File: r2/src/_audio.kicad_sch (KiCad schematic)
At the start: 27 parts, among them J1 532610271, J5 PJ-320D, U4 PCM5100APW, U5 PAM8908

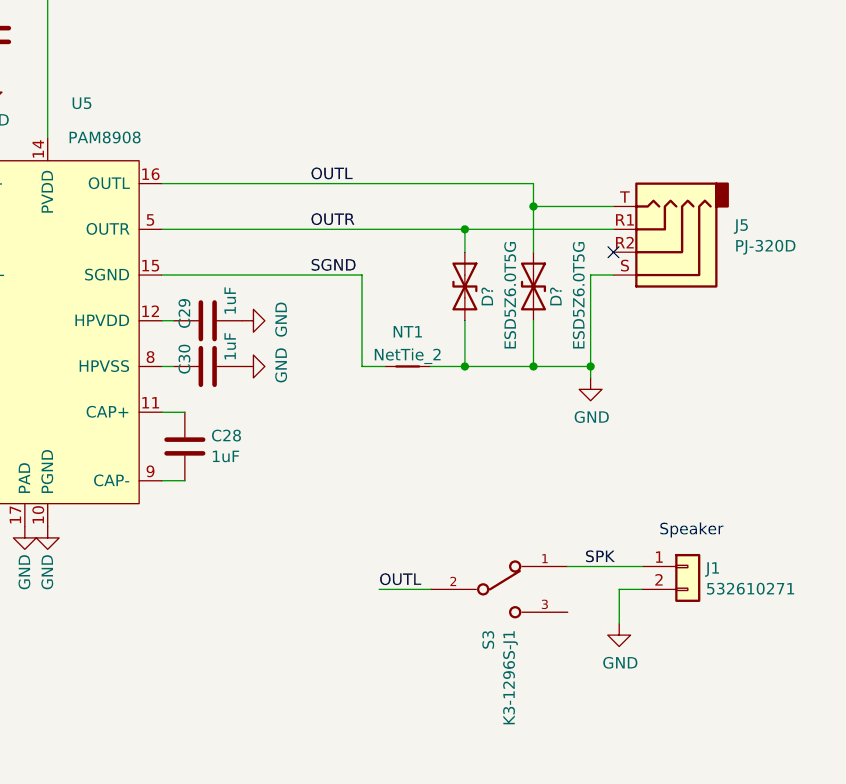
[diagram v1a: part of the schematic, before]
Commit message: Correct switch symbol so default switch behaviour from factory is correctly shown.
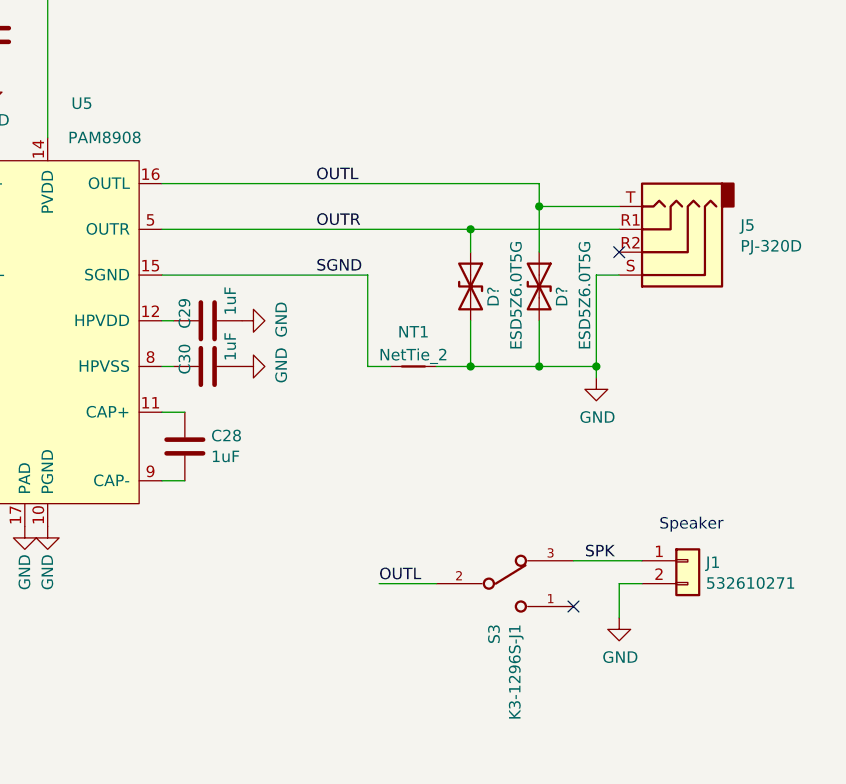
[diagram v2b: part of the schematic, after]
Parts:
- S3: symbol j_Switch:JS102011SAQN -> j_Switch:K3-1296S; MPN K3-1296S-J1 -> K3-1296S
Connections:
- net SPK: now also S3.3; no longer S3.1
- no-connect marks 1 -> 2
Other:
- moved on the sheet: D?, J1, J5, NT1, S3

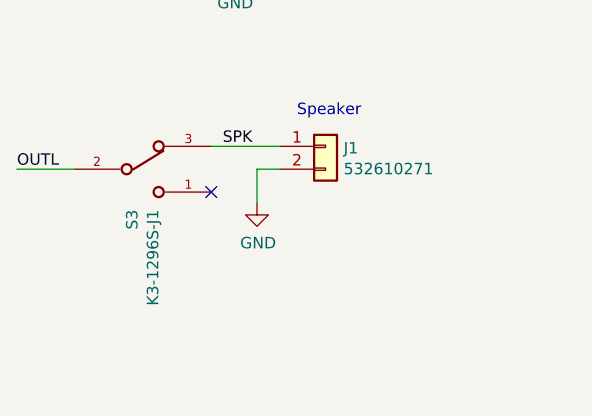
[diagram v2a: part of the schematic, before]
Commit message: Change speaker connector symbol to include mounting pads. Add speaker symbol and footprint
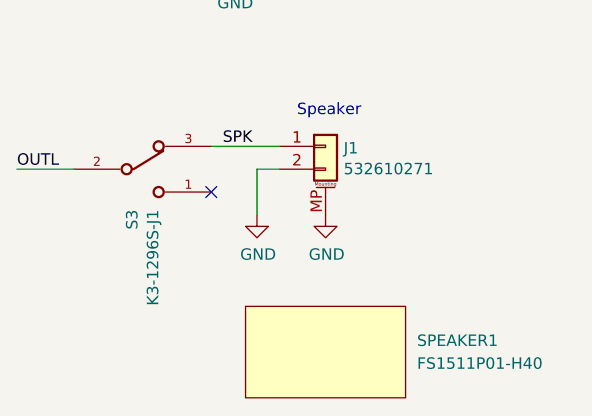
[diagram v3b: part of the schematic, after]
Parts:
- added SPEAKER1: FS1511P01-H40, jeffmakes-footprints:FS1511P01-Hx-Lx, symbol j_Display:Display_dummy
- J1: symbol Connector_Generic:Conn_01x02 -> Connector_Generic_MountingPin:Conn_01x02_MountingPin
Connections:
- net GND: now also J1.MP (MountPin)
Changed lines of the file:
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@@
     (stroke (width 0) (type default))
   )
-  (wire (pts (xy 243.84 127) (xy 243.84 130.81))
+  (wire (pts (xy 243.84 127) (xy 243.84 132.08))
     (stroke (width 0) (type default))
   )
@@
     )
   )
-  (symbol (lib_id "power:GND") (at 243.84 130.81 0) (unit 1)
-    (in_bom yes) (on_board yes) (dnp no)
-    (property "Reference" "#PWR0154" (at 243.84 137.16 0)
-      (effects (font (size 1.27 1.27)) hide)
-    )
-    (property "Value" "GND" (at 243.967 135.2042 0)
-      (effects (font (size 1.27 1.27)))
-    )
-    (property "Footprint" "" (at 243.84 130.81 0)
-      (effects (font (size 1.27 1.27)) hide)
-    )
-    (property "Datasheet" "" (at 243.84 130.81 0)
+  (symbol (lib_id "power:GND") (at 251.46 132.08 0) (unit 1)
+    (in_bom yes) (on_board yes) (dnp no)
+    (property "Reference" "#PWR0155" (at 251.46 138.43 0)
+      (effects (font (size 1.27 1.27)) hide)
+    )
+    (property "Value" "GND" (at 251.587 136.4742 0)
+      (effects (font (size 1.27 1.27)))
+    )
+    (property "Footprint" "" (at 251.46 132.08 0)
+      (effects (font (size 1.27 1.27)) hide)
+    )
+    (property "Datasheet" "" (at 251.46 132.08 0)
+      (effects (font (size 1.27 1.27)) hide)
+    )
+    (pin "1")
+    (instances
+      (project "tr23-badge-r2"
+        (path "/ab725fe7-4504-40ef-b6af-82d065d00fb6/00000000-0000-0000-0000-00005dd6a7f2"
+          (reference "#PWR0155") (unit 1)
+        )
+      )
+    )
+  )
+  (symbol (lib_id "power:GND") (at 243.84 132.08 0) (unit 1)
+    (in_bom yes) (on_board yes) (dnp no)
+    (property "Reference" "#PWR0154" (at 243.84 138.43 0)
+      (effects (font (size 1.27 1.27)) hide)
+    )
+    (property "Value" "GND" (at 243.967 136.4742 0)
+      (effects (font (size 1.27 1.27)))
+    )
+    (property "Footprint" "" (at 243.84 132.08 0)
+      (effects (font (size 1.27 1.27)) hide)
+    )
+    (property "Datasheet" "" (at 243.84 132.08 0)
       (effects (font (size 1.27 1.27)) hide)
     )
@@
     )
   )
-  (symbol (lib_id "Connector_Generic:Conn_01x02") (at 251.46 124.46 0) (unit 1)
+  (symbol (lib_id "j_Display:Display_dummy") (at 251.46 147.32 0) (unit 1)
+    (in_bom yes) (on_board yes) (dnp no) (fields_autoplaced)
+    (property "Reference" "SPEAKER1" (at 261.62 146.05 0)
+      (effects (font (size 1.27 1.27)) (justify left))
+    )
+    (property "Value" "FS1511P01-H40" (at 261.62 148.59 0)
+      (effects (font (size 1.27 1.27)) (justify left))
+    )
+    (property "Footprint" "jeffmakes-footprints:FS1511P01-Hx-Lx" (at 251.46 147.32 0)
+      (effects (font (size 1.27 1.27)) hide)
+    )
+    (property "Datasheet" "" (at 251.46 147.32 0)
+      (effects (font (size 1.27 1.27)) hide)
+    )
+    (instances
+      (project "tr23-badge-r2"
+        (path "/ab725fe7-4504-40ef-b6af-82d065d00fb6/00000000-0000-0000-0000-00005dd6a7f2"
+          (reference "SPEAKER1") (unit 1)
+        )
+      )
+    )
+  )
+  (symbol (lib_id "Connector_Generic_MountingPin:Conn_01x02_MountingPin") (at 251.46 124.46 0) (unit 1)
     (in_bom yes) (on_board yes) (dnp no)
     (property "Reference" "J1" (at 253.4666 124.6632 0)
@@
     (pin "1")
     (pin "2")
-    (instances
-      (project "tr23-badge-r2"
+    (pin "MP")
+    (instances
+      (project "tr23-badge-r2"

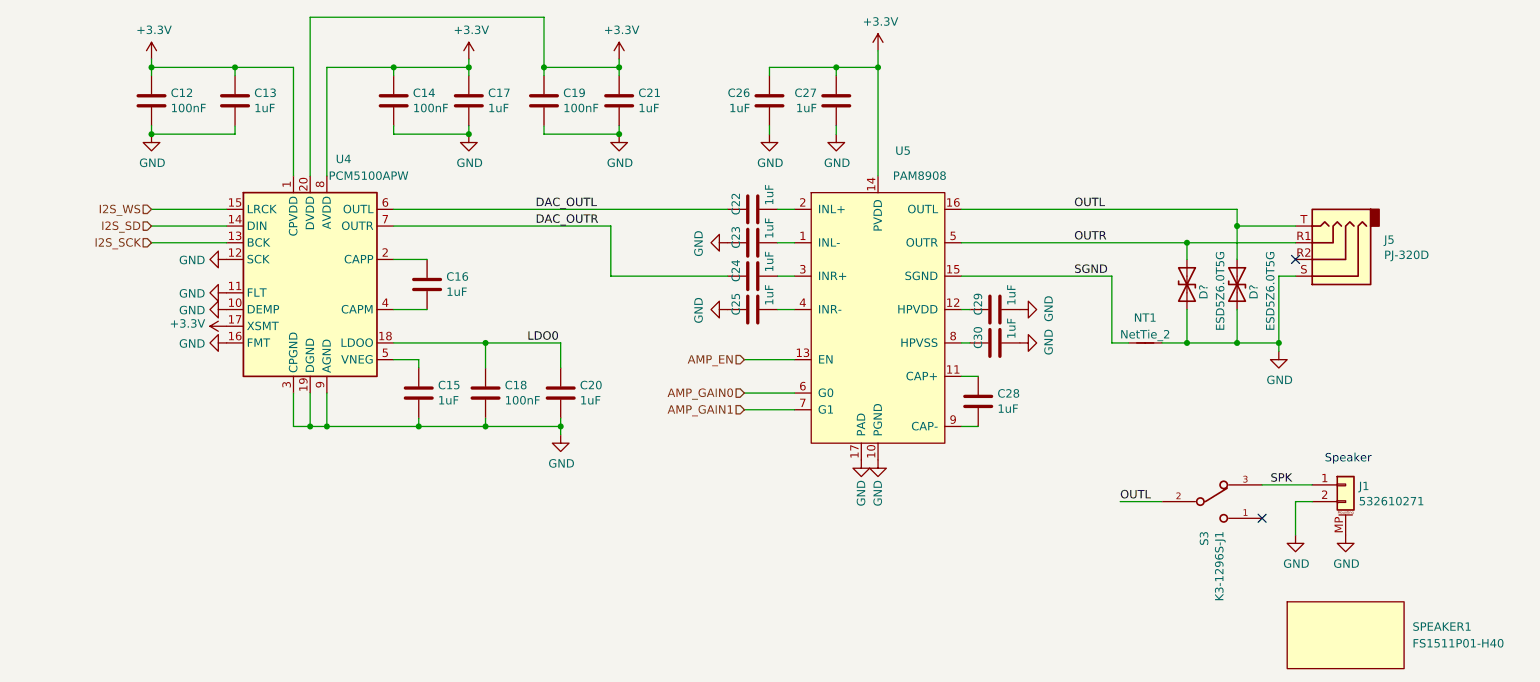
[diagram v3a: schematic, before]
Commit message: Add pull-downs to amplifier enable/gain control lines
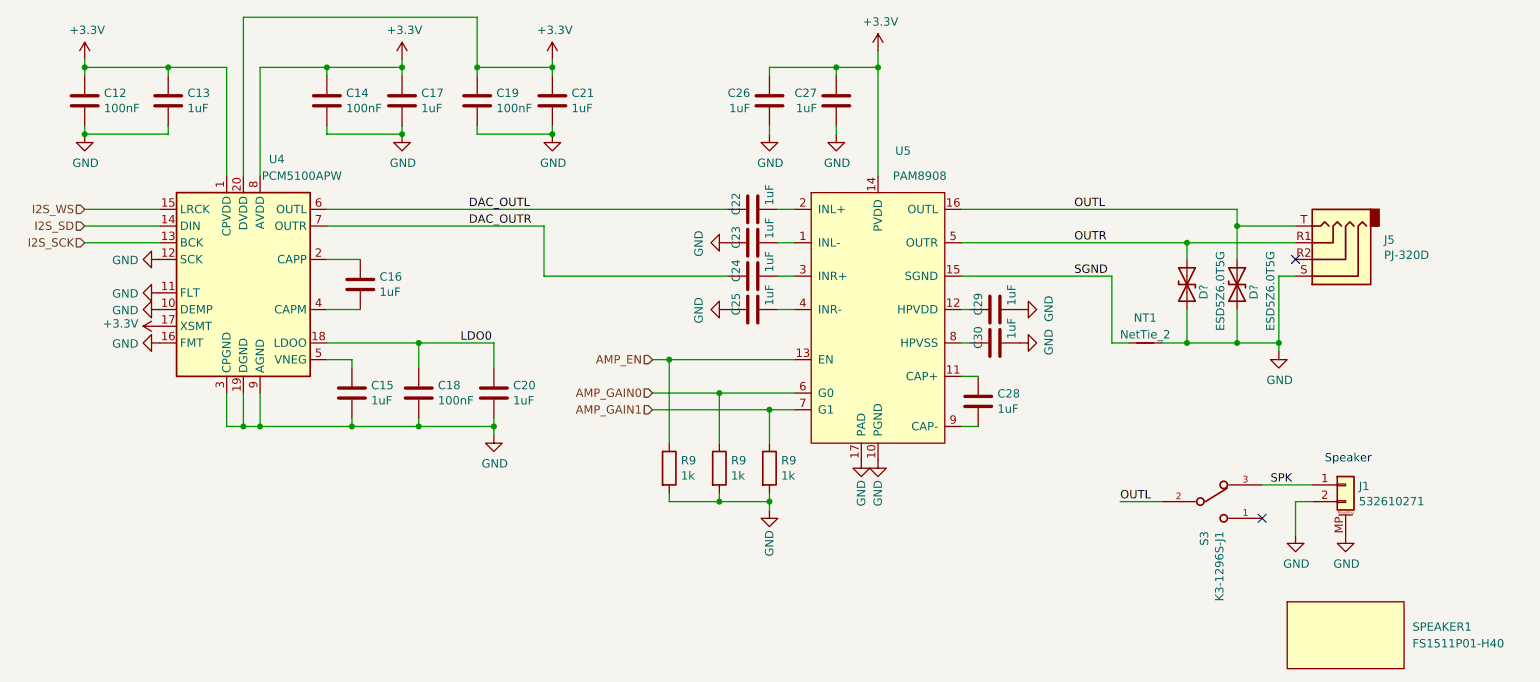
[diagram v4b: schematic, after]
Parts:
- added R9 (x3): 1k, Resistor_SMD:R_0402_1005Metric, symbol Device:R
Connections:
- net AMP_EN: now also R9.1
- net AMP_GAIN0: now also R9.1
- net AMP_GAIN1: now also R9.1
- net GND: now also R9.2, R9.2, R9.2
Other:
- moved on the sheet: C12, C13, C14, C15, C16, C17, C18, C19, C20, C21, U4

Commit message: Rename speaker footprint
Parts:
- SPEAKER1: footprint jeffmakes-footprints:FS1511P01-Hx-Lx -> jeffmakes-footprints:FS1511P01
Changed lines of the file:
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@@
       (effects (font (size 1.27 1.27)) (justify left))
     )
-    (property "Footprint" "jeffmakes-footprints:FS1511P01-Hx-Lx" (at 251.46 147.32 0)
+    (property "Footprint" "jeffmakes-footprints:FS1511P01" (at 251.46 147.32 0)
       (effects (font (size 1.27 1.27)) hide)
     )

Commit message: Set title block contents
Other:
- company: (none) -> Monad Gottfried Ltd. 2023
- title: (none) -> Troopers 23 Badge
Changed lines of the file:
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@@
 (kicad_sch (version 20230409) (generator eeschema)
   (paper "A4")
+  (title_block
+    (title "Troopers 23 Badge")
+    (rev "r2")
+    (company "Monad Gottfried Ltd. 2023")
+    (comment 1 "for ERNW Enno Rey Netzwerke GmbH")
+  )
   (junction (at 83.82 115.57) (diameter 0) (color 0 0 0 0)
   )

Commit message: Change speaker part number to -35 variant, I think the -40 may have been discontinued, and I doubt it makes much odds
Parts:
- SPEAKER1: value FS1511P01-H40 -> FS1511P01-H35
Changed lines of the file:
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@@
       (effects (font (size 1.27 1.27)) (justify left))
     )
-    (property "Value" "FS1511P01-H40" (at 261.62 148.59 0)
+    (property "Value" "FS1511P01-H35" (at 261.62 148.59 0)
       (effects (font (size 1.27 1.27)) (justify left))
     )
